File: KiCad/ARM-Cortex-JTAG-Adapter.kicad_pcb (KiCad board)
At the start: 2 copper layers, 36.1 x 30.5 mm, 5 parts, among them J1 M20-9990646, J2 M20-9990346

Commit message: Updating the version number.
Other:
- board text added: "JLink Cortex-M/A Rev 0.1B"
- board text removed: "JLink Cortex-M/A Rev 0.1A"

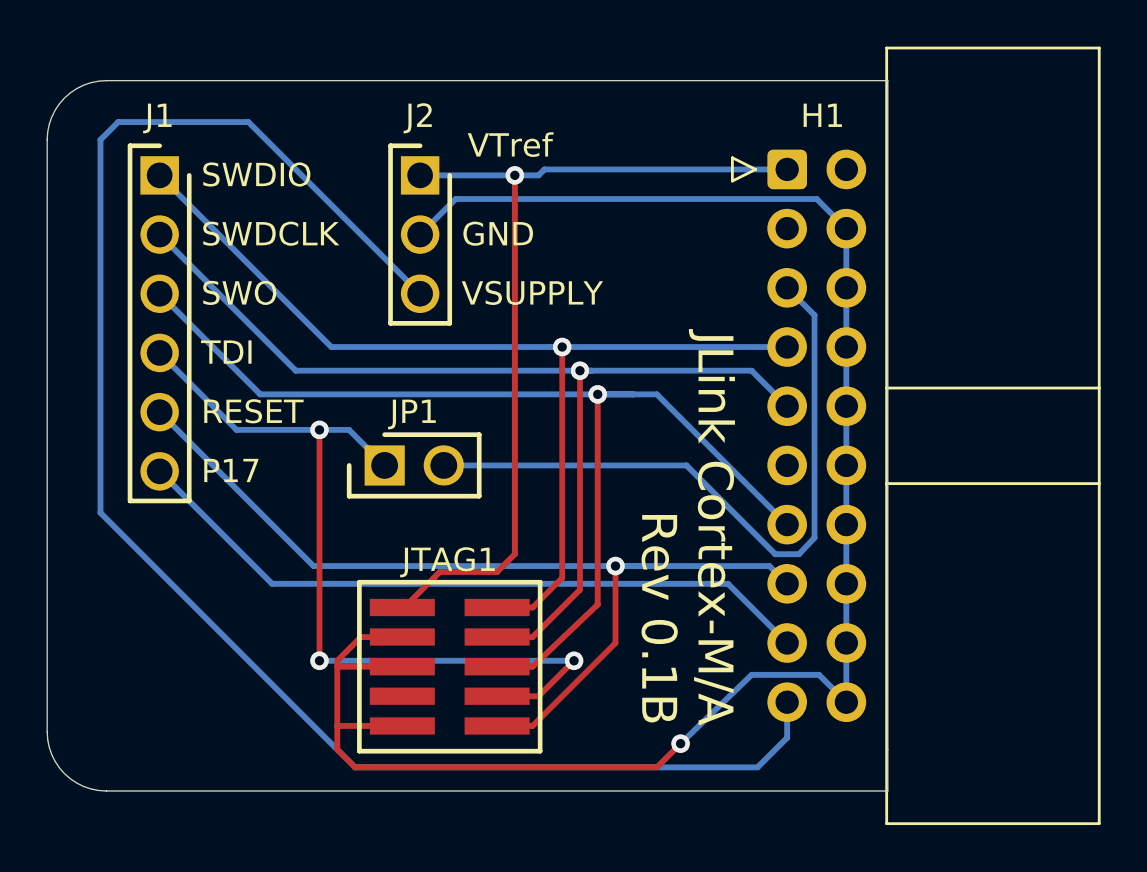
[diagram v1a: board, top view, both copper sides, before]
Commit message: Flipped the H1 connector layout.
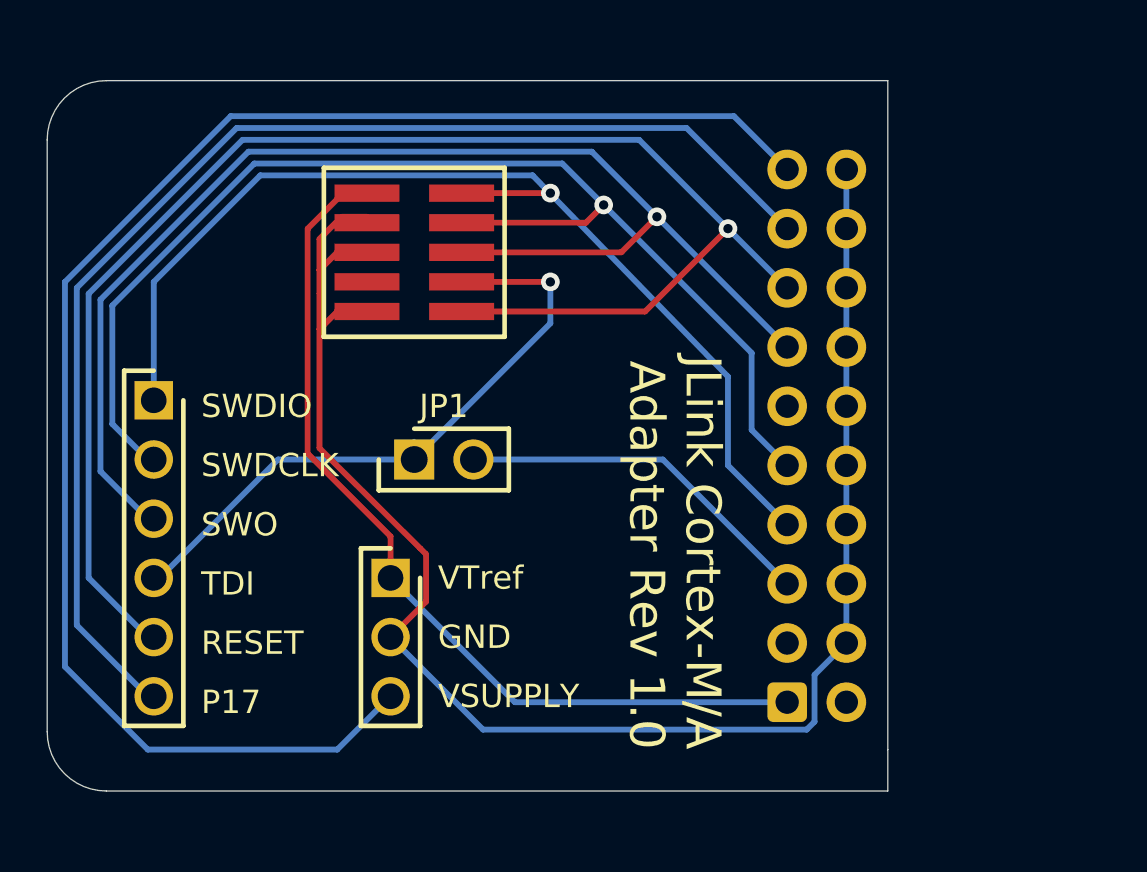
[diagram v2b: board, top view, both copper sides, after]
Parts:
- H1: moved to B.Cu
- moved H1 22.9 mm to (159.0, 133.6)
- moved JTAG1 17.8 mm to (143.0, 114.3)
- moved J2 17.3 mm to (142.0, 128.3)
- moved J1 9.66 mm to (131.8, 120.7)
- moved JP1 1.30 mm to (143.0, 123.2)
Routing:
- net /P17: track 30.0 -> 54.3 mm
- net /RESET: track 40.7 -> 64.4 mm
- net /TDI: track 29.0 -> 15.7 mm
- net /SWDCLK: track 44.4 -> 52.8 mm
- net /TDI_IN: track 36.2 -> 28.0 mm, vias 3 -> 1
- net /SWO: track 47.0 -> 55.2 mm
- net /GND: track 76.9 -> 72.0 mm, vias 1 -> 0
- net /SWDIO: track 43.3 -> 46.7 mm
- net /5V: track 69.1 -> 67.8 mm
- net /VTref: track 37.8 -> 38.9 mm, vias 1 -> 0
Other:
- rule pad_to_mask_clearance: 0.05 -> 0
- board text added: "JLink Cortex-M/A Adapter Rev 1.0"
- board text removed: "JLink Cortex-M/A Rev 0.1B"

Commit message: Adding Adafruit SWD connector module.
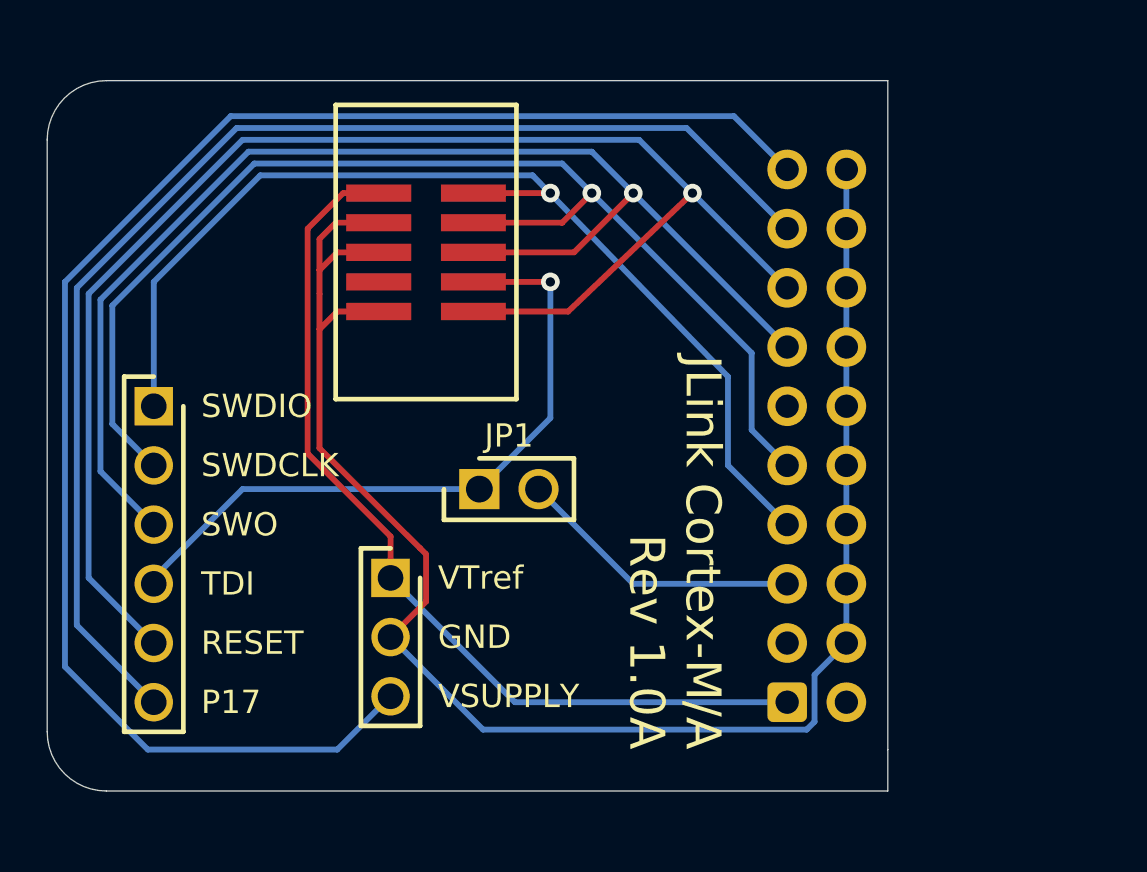
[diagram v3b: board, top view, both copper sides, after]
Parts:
- JTAG1: value FTSH-105-01-L-DV-K -> 485-752; footprint (Local):SAMTEC-FTSH-105-01-X-DV -> (Local):Adafruit_SWD_Connector_PID_752
- moved JP1 3.07 mm to (145.8, 124.5)
- moved JTAG1 0.51 mm to (143.5, 114.3)
- moved J1 0.25 mm to (131.8, 120.9)
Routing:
- net /TDI: track 15.7 -> 12.4 mm
- net /RESET: track 64.4 -> 62.9 mm
- net /SWO: track 55.2 -> 54.1 mm
- net /TDI_IN: track 28.0 -> 29.0 mm
- net /SWDCLK: track 52.8 -> 52.0 mm
- net /VTref: track 38.9 -> 39.4 mm
- net /SWDIO: track 46.7 -> 46.2 mm
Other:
- board text added: "JLink Cortex-M/A Rev 1.0A"
- board text removed: "JLink Cortex-M/A Adapter Rev 1.0"
